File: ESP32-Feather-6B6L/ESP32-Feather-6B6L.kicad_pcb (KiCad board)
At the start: 2 copper layers, 86.4 x 76.2 mm, 36 parts, among them J201 RJ45, J202 RJ45, J401 1 2 3 4 5 6 G, J501 + 1 2 3 4 5 6 -, U201 TCAN332DR, U301 LM2574N-5.0, U403 74HCT14, U501 TBD62084A

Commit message: Final through-hole tweaks.
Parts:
- moved J201 2.54 mm to (178.3, 43.6)
- moved J501 1.86 mm to (133.3, 41.4)
- moved R502 1.86 mm to (138.7, 59.1)
- moved R503 1.86 mm to (138.7, 56.6)
- moved R504 1.86 mm to (138.7, 54.0)
- moved R505 1.86 mm to (138.7, 51.5)
- moved R501 1.86 mm to (138.7, 61.6)
- moved R506 1.86 mm to (138.7, 48.9)
- moved R507 1.86 mm to (138.7, 43.9)
- moved R508 1.86 mm to (138.7, 46.4)
- moved U501 1.86 mm to (157.5, 61.6)
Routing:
- net /CAN Transceiver/CANH: track 67.9 -> 70.5 mm
- net /CAN Transceiver/+12V CAN Power: track 69.2 -> 71.8 mm
- net Net-(J201-Pad5): track 54.1 -> 56.7 mm
- net Net-(J201-Pad4): track 48.0 -> 50.6 mm
- net /CAN Transceiver/CANL: track 62.4 -> 64.9 mm
- net /N$19: track 15.8 -> 17.7 mm
- net /N$3: track 15.2 -> 17.1 mm
- net /N$5: track 15.2 -> 17.1 mm
- net /N$21: track 19.3 -> 21.1 mm
- net /N$24: track 31.4 -> 33.3 mm
- net /N$20: track 16.5 -> 18.4 mm
- net /N$23: track 26.7 -> 28.5 mm
- net /N$22: track 21.6 -> 23.4 mm
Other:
- board size 86.4 x 76.2 mm -> 86.4 x 78.7 mm

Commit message: Final through-hole tweaks.
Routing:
- net Net-(R505-Pad1): track 0.00 -> 5.43 mm
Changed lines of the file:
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@@
   (segment (start 143.256 41.3188) (end 149.86 41.3188) (width 1) (layer "B.Cu") (net 39))
   (segment (start 141.65 64.2608) (end 141.732 64.1788) (width 1) (layer "B.Cu") (net 39))
+  (segment (start 133.37 43.8588) (end 133.288 43.9408) (width 0.5) (layer "B.Cu") (net 40))
   (segment (start 138.684 43.8588) (end 133.37 43.8588) (width 0.5) (layer "B.Cu") (net 40))
-  (segment (start 133.37 43.8588) (end 133.288 43.9408) (width 0.5) (layer "B.Cu") (net 40))
+  (segment (start 138.684 46.3988) (end 133.37 46.3988) (width 0.5) (layer "B.Cu") (net 41))
   (segment (start 133.37 46.3988) (end 133.288 46.4808) (width 0.5) (layer "B.Cu") (net 41))
-  (segment (start 138.684 46.3988) (end 133.37 46.3988) (width 0.5) (layer "B.Cu") (net 41))
   (segment (start 138.684 56.5588) (end 133.37 56.5588) (width 0.5) (layer "B.Cu") (net 42))
   (segment (start 133.37 56.5588) (end 133.288 56.6408) (width 0.5) (layer "B.Cu") (net 42))
@@
   (segment (start 146.304 43.8588) (end 149.86 43.8588) (width 0.5) (layer "B.Cu") (net 53))
   (segment (start 149.86 46.3988) (end 146.304 46.3988) (width 0.5) (layer "B.Cu") (net 54))
-  (segment (start 133.37 48.9388) (end 133.288 49.0208) (width 0.25) (layer "B.Cu") (net 55))
-  (segment (start 138.684 48.9388) (end 133.37 48.9388) (width 0.25) (layer "B.Cu") (net 55))
-  (segment (start 138.684 54.0188) (end 133.37 54.0188) (width 0.25) (layer "B.Cu") (net 57))
-  (segment (start 133.37 54.0188) (end 133.288 54.1008) (width 0.25) (layer "B.Cu") (net 57))
-  (segment (start 133.37 59.0988) (end 133.288 59.1808) (width 0.25) (layer "B.Cu") (net 58))
-  (segment (start 138.684 59.0988) (end 133.37 59.0988) (width 0.25) (layer "B.Cu") (net 58))
-  (segment (start 138.684 61.6388) (end 133.37 61.6388) (width 0.25) (layer "B.Cu") (net 59))
-  (segment (start 133.37 61.6388) (end 133.288 61.7208) (width 0.25) (layer "B.Cu") (net 59))
+  (segment (start 133.37 48.9388) (end 133.288 49.0208) (width 0.5) (layer "B.Cu") (net 55))
+  (segment (start 138.684 48.9388) (end 133.37 48.9388) (width 0.5) (layer "B.Cu") (net 55))
+  (segment (start 133.37 51.4788) (end 133.288 51.5608) (width 0.5) (layer "B.Cu") (net 56))
+  (segment (start 138.684 51.4788) (end 133.37 51.4788) (width 0.5) (layer "B.Cu") (net 56))
+  (segment (start 133.37 54.0188) (end 133.288 54.1008) (width 0.5) (layer "B.Cu") (net 57))
+  (segment (start 138.684 54.0188) (end 133.37 54.0188) (width 0.5) (layer "B.Cu") (net 57))
+  (segment (start 138.684 59.0988) (end 133.37 59.0988) (width 0.5) (layer "B.Cu") (net 58))
+  (segment (start 133.37 59.0988) (end 133.288 59.1808) (width 0.5) (layer "B.Cu") (net 58))
+  (segment (start 133.37 61.6388) (end 133.288 61.7208) (width 0.5) (layer "B.Cu") (net 59))
+  (segment (start 138.684 61.6388) (end 133.37 61.6388) (width 0.5) (layer "B.Cu") (net 59))
   (zone (net 27) (net_name "+3V3") (layer "F.Cu") (hatch edge 0.508)
     (connect_pads (clearance 0.508))

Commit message: Final through-hole tweaks.
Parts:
- J401: value 1 2 3 4 5 6 G -> G 6 5 4 3 2 1
- J501: value + 1 2 3 4 5 6 - -> + 1 2 3 4 5 6 7 8 -

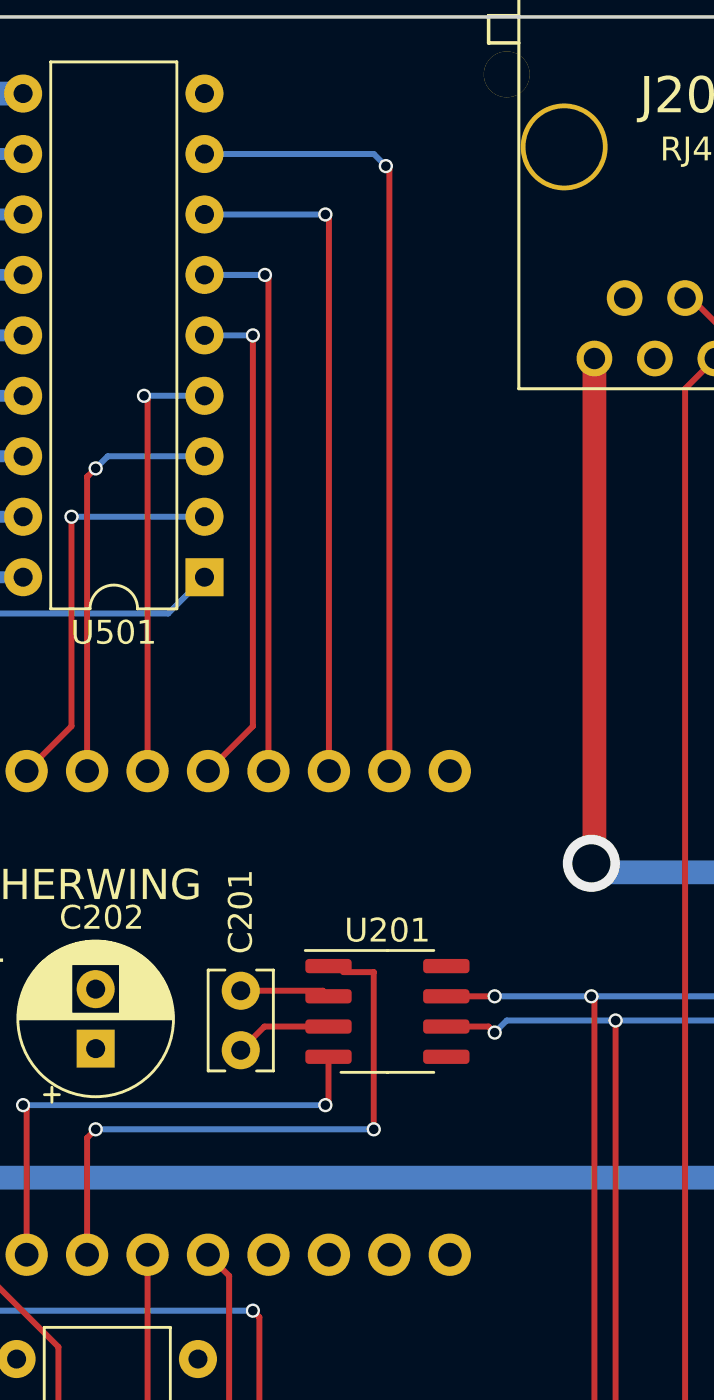
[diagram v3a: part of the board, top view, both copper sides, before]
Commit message: Rescue SCL.
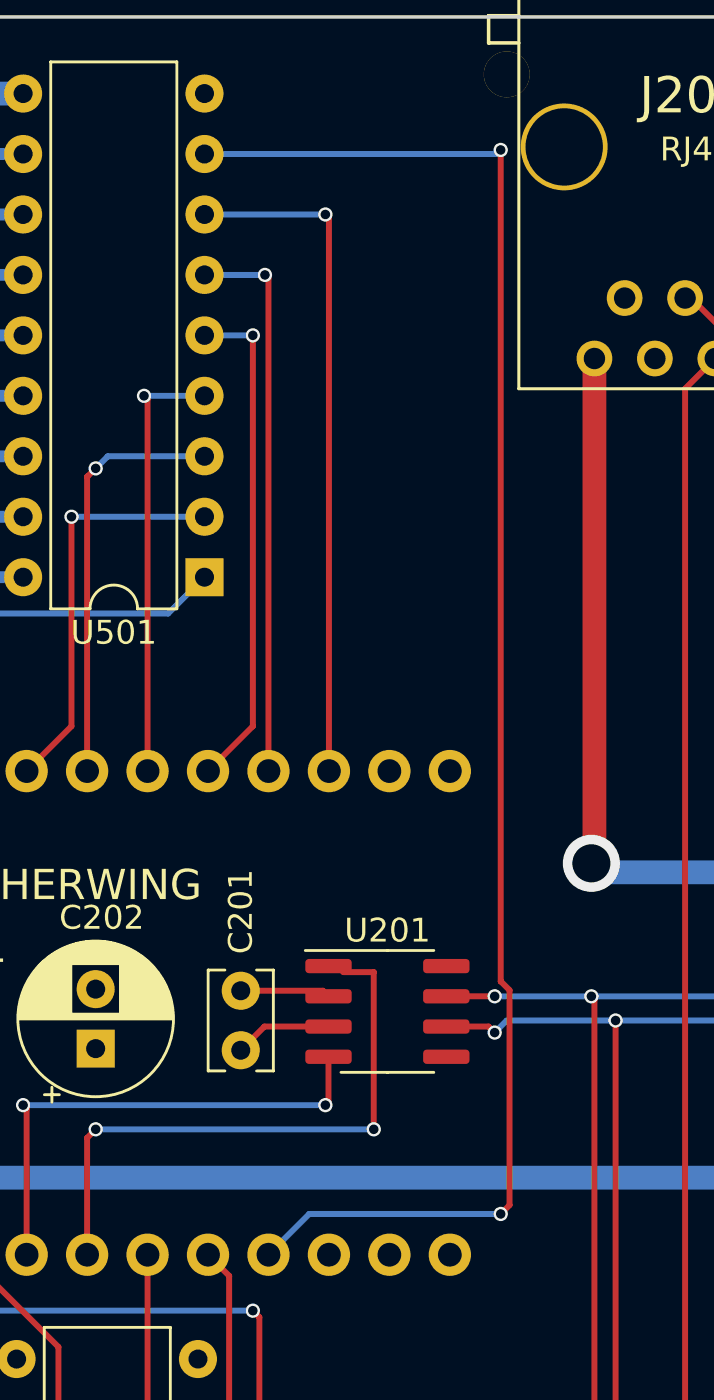
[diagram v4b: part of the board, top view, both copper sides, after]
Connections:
- U501 pad 8: /N$24 -> /N$7
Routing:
- net /N$7: track 0.00 -> 68.0 mm, vias 0 -> 2
- net /N$24: track 33.3 -> 0.00 mm, vias 1 -> 0
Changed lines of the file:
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@@
       (net 3 "/N$23") (pinfunction "In") (pintype "input"))
     (pad "8" thru_hole oval (at 0 17.78 180) (size 1.6 1.6) (drill 0.8) (layers *.Cu *.Mask)
-      (net 2 "/N$24") (pinfunction "In") (pintype "input"))
+      (net 20 "/N$7") (pinfunction "In") (pintype "input"))
     (pad "9" thru_hole oval (at 0 20.32 180) (size 1.6 1.6) (drill 0.8) (layers *.Cu *.Mask)
       (net 24 "GND") (pinfunction "IC") (pintype "unspecified"))
@@
   )
   (gr_rect (start 213.36 116.84) (end 127 38.1) (layer "Edge.Cuts") (width 0.15) (fill none))
-  (segment (start 165.2484 44.5152) (end 165.1 44.3668) (width 0.25) (layer "F.Cu") (net 2))
-  (segment (start 165.2484 69.7848) (end 165.2484 44.5152) (width 0.25) (layer "F.Cu") (net 2))
-  (via (at 165.1 44.3668) (size 0.6) (drill 0.4) (layers "F.Cu" "B.Cu") (net 2))
-  (segment (start 165.1 44.3668) (end 164.592 43.8588) (width 0.25) (layer "B.Cu") (net 2))
-  (segment (start 164.592 43.8588) (end 157.48 43.8588) (width 0.25) (layer "B.Cu") (net 2))
   (segment (start 162.7084 69.7848) (end 162.7084 46.5472) (width 0.25) (layer "F.Cu") (net 3))
   (segment (start 162.7084 46.5472) (end 162.56 46.3988) (width 0.25) (layer "F.Cu") (net 3))
@@
   (segment (start 157.6284 90.1048) (end 158.517399 90.993799) (width 0.25) (layer "F.Cu") (net 19))
   (segment (start 158.517399 90.993799) (end 158.517399 100.796601) (width 0.25) (layer "F.Cu") (net 19))
+  (segment (start 169.930884 78.623) (end 170.297 78.989116) (width 0.25) (layer "F.Cu") (net 20))
+  (segment (start 170.297 88.021) (end 169.926 88.392) (width 0.25) (layer "F.Cu") (net 20))
+  (segment (start 170.297 78.989116) (end 170.297 88.021) (width 0.25) (layer "F.Cu") (net 20))
+  (segment (start 169.926 43.688) (end 169.926 78.623) (width 0.25) (layer "F.Cu") (net 20))
+  (segment (start 169.926 78.623) (end 169.930884 78.623) (width 0.25) (layer "F.Cu") (net 20))
+  (via (at 169.926 43.688) (size 0.6) (drill 0.4) (layers "F.Cu" "B.Cu") (net 20))
+  (via (at 169.926 88.392) (size 0.6) (drill 0.4) (layers "F.Cu" "B.Cu") (net 20))
+  (segment (start 169.7552 43.8588) (end 157.48 43.8588) (width 0.25) (layer "B.Cu") (net 20))
+  (segment (start 169.926 43.688) (end 169.7552 43.8588) (width 0.25) (layer "B.Cu") (net 20))
+  (segment (start 160.1684 90.1048) (end 161.8812 88.392) (width 0.25) (layer "B.Cu") (net 20))
+  (segment (start 161.8812 88.392) (end 169.926 88.392) (width 0.25) (layer "B.Cu") (net 20))
   (segment (start 144.586 97.028) (end 146.304 98.746) (width 0.25) (layer "F.Cu") (net 24))
   (segment (start 162.456 79.014) (end 159.004 79.014) (width 0.25) (layer "F.Cu") (net 24))
